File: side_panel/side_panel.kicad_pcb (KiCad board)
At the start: 2 copper layers, 88 parts, among them CN4 DLL-5569-6AW, CN5 KF2EDGRC-5.08-4P, SW15 KH-6X6X6H-STM, SW16 KH-6X6X6H-STM, U19 PY32F030K28U6TR, U20 WAFER-XH254WZ-2A, U21 WAFER-XH254WZ-2A, U22 WAFER-XH254WZ-4A, U23 KF128-5.08-2P, U24 KF128-5.08-2P, U31 TMC2209-LA, U32 VL53L0CXV0DH1, U33 TPS562201DDCR, U34 SS6285M-SO-TP, U35 SP3485EN, X3 AFA01-S05FCA-00, X4 AFA01-S05FCA-00

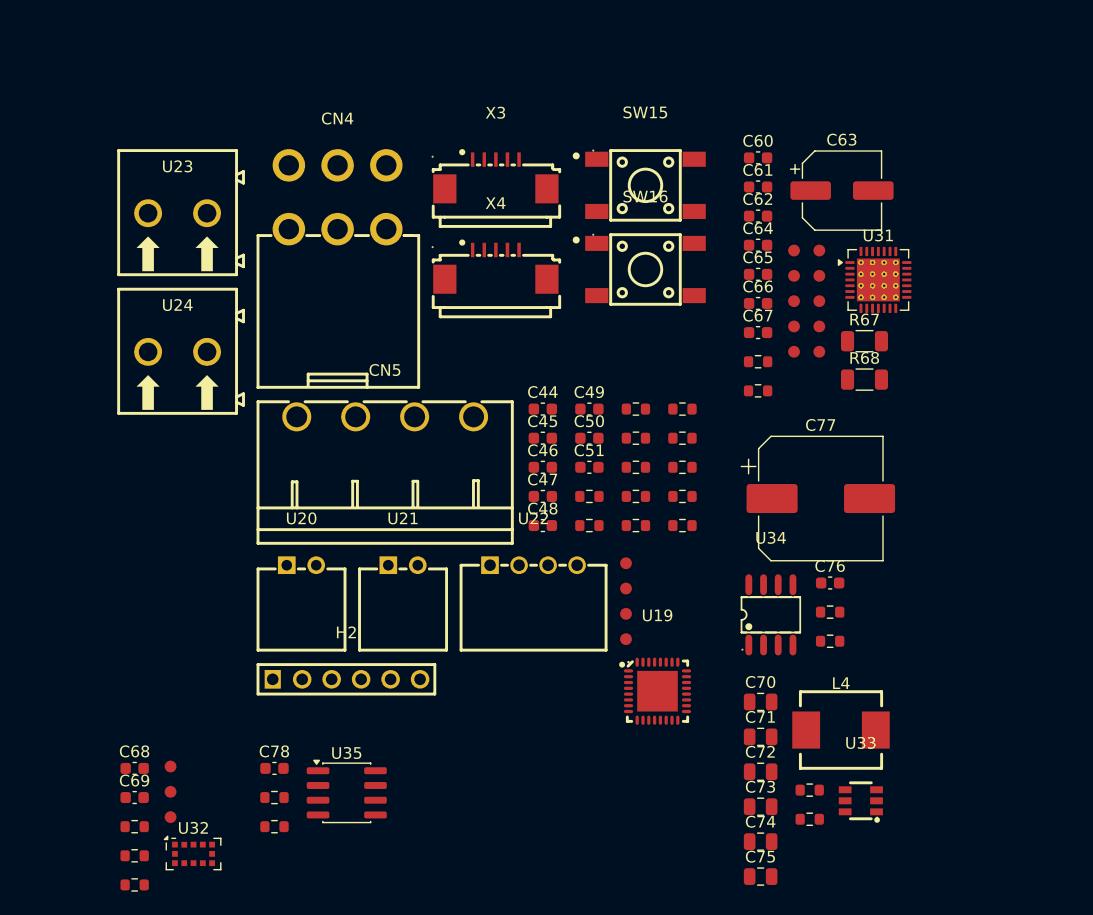
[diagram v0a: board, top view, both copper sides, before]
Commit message: feat: 添加侧电机板基础元件布局
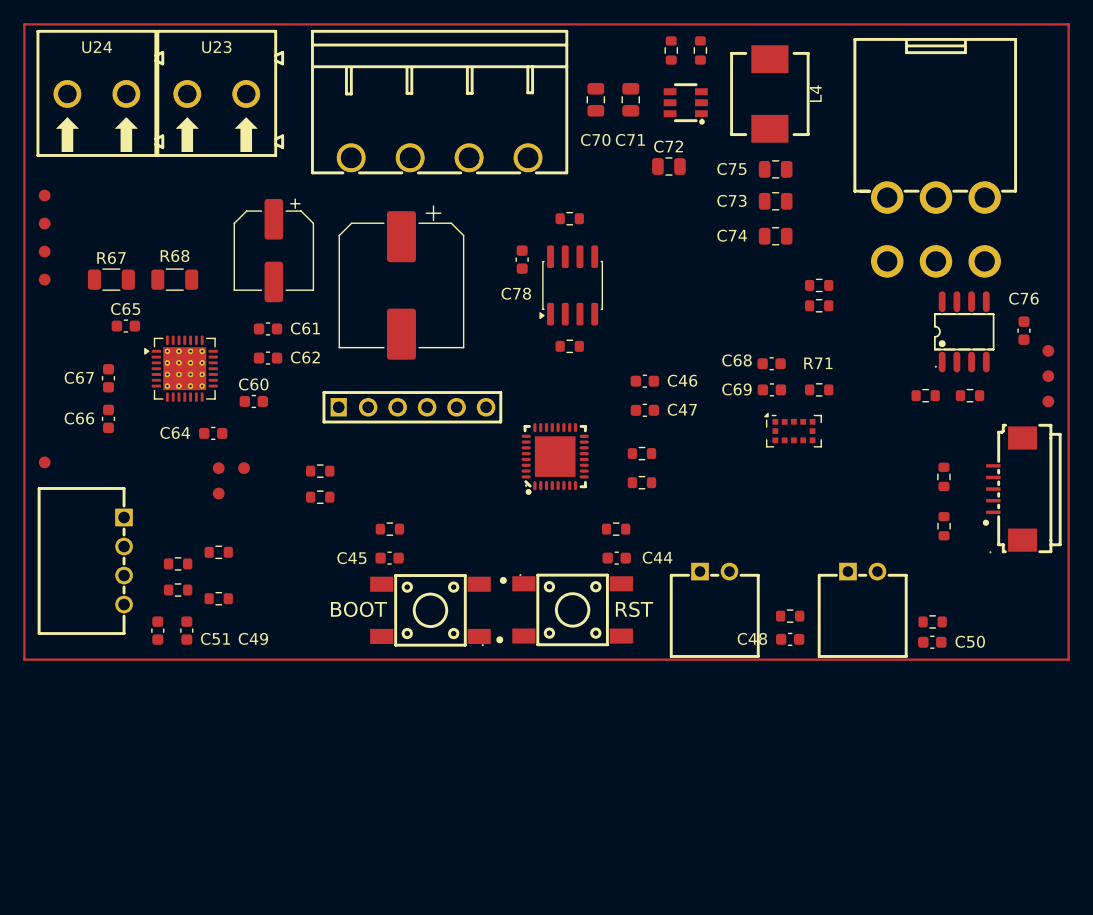
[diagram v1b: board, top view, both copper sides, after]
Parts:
- removed TP14, TP15, TP16, TP17: 1.0mm, PCM_SparkFun-Connector:TestPoint-1.0mm
- removed TP24, TP25: TestPoint, PCM_SparkFun-Connector:TestPoint-1.0mm
- removed X4: AFA01-S05FCA-00, lcsc_footprints:C262753_FPC-SMD_AFA01-S05FCA-00
- moved TP32 83.7 mm to (180.2, 83.4)
- moved TP33 83.7 mm to (180.2, 85.6)
- moved TP34 83.7 mm to (180.2, 87.8)
- moved R69 76.0 mm to (171.2, 94.2), turned to -90 degrees
- moved R70 75.3 mm to (171.3, 98.5), turned to 90 degrees
- moved R71 72.8 mm to (160.5, 86.8)
- moved TP29 67.4 mm to (93.8, 70.0)
- moved TP31 67.3 mm to (93.8, 74.8)
- moved R73 66.9 mm to (150.3, 57.5), turned to 90 degrees
- moved TP28 66.9 mm to (93.8, 72.4)
- moved TP30 66.9 mm to (93.8, 77.2)
- moved TP26 65.3 mm to (93.8, 93.0)
- moved C69 65.2 mm to (156.4, 86.8)
- moved R67 65.1 mm to (99.5, 77.2)
- moved C68 65.0 mm to (156.4, 84.5)
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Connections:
- R65 pad 2: /步进驱动/UART_TX/RX -> /TMC_UART
- R66 pad 1: /步进驱动/EN -> /TMC_EN
- R71 pad 1: /TOF/XSHUT -> /TOF_XSHUT
- TP23 pad 1: /步进驱动/DIR -> /TMC_DIR
- U19 pad 10: /MOTOR_BI -> /TOF_XSHUT
- U19 pad 11: Net-(U19-PA5) -> /SCL
- U19 pad 12: /TMC_STEP -> /SDA
- U19 pad 13: /MOTOR_FI -> /MOTOR_ENC_B
- U19 pad 14: /步进驱动/DIAG -> /MOTOR_ENC_A
- U19 pad 15: Net-(U19-PB1) -> unconnected-(U19-PB1-Pad15)
- U19 pad 17: /RS485_PY32/RS485_DE -> /MOTOR_FI
- U19 pad 18: /EXT_ENC_A -> /MOTOR_BI
- U19 pad 19: /EXT_ENC_B -> unconnected-(U19-PA9-OSC32OUT-Pad19)
- U19 pad 2: /步进驱动/EN -> /EXT_ENC_B
- U19 pad 20: /PUSH_BUTTON_2 -> /RS485_PY32/RS485_TX
- U19 pad 21: /TOF_SCL -> /RS485_PY32/RS485_RX
- U19 pad 22: /TOF_SDA -> /RS485_PY32/RS485_DE
- U19 pad 26: Net-(U19-PB3) -> /TMC_DIAG
- U19 pad 27: /MOTOR_ENC_A -> /TMC_UART
- U19 pad 28: /MOTOR_ENC_B -> /TMC_EN
- U19 pad 29: /RS485_PY32/RS485_TX -> /TMC_DIR
- U19 pad 3: /步进驱动/UART_TX/RX -> /EXT_ENC_A
- U19 pad 30: /RS485_PY32/RS485_RX -> /TMC_STEP
- U19 pad 32: Net-(U19-PB8) -> unconnected-(U19-PB8-Pad32)
- U19 pad 5: /步进驱动/DIR -> /PUSH_BUTTON_1
- U19 pad 7: /TOF_XSHUT -> /PUSH_BUTTON_2
- U19 pad 8: /步进驱动/INDEX -> unconnected-(U19-PA2-Pad8)
- U19 pad 9: /PUSH_BUTTON_1 -> unconnected-(U19-PA3-Pad9)
- U31 pad 11: /步进驱动/DIAG -> /TMC_DIAG
- U31 pad 19: /步进驱动/DIR -> /TMC_DIR
- U31 pad 2: /步进驱动/EN -> /TMC_EN
- U32 pad 5: /TOF/XSHUT -> /TOF_XSHUT
- U34 pad 5: /MOTOR_OUT2 -> /MOTOR_OUT1
- U34 pad 6: /MOTOR_OUT2 -> /MOTOR_OUT1
- U34 pad 7: /MOTOR_OUT1 -> /MOTOR_OUT2
- U34 pad 8: /MOTOR_OUT1 -> /MOTOR_OUT2
- X3 pad 1: /TOF/XSHUT -> /TOF_XSHUT
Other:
- board text added: "BOOT"
- board text added: "RST"

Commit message: update: 更新侧板PCB
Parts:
- moved C64 4.76 mm to (112.2, 87.8), turned to -90 degrees
- moved C60 1.18 mm to (110.6, 87.8), turned to -90 degrees
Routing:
- net /TMC_UART: track 0.00 -> 17.8 mm
- net /SWDIO: track 0.00 -> 15.7 mm
- net /RST: track 0.00 -> 12.8 mm, vias 0 -> 2
- net Net-(U31-~{PD}/UART): track 0.00 -> 12.5 mm
- net /SWCLK: track 0.00 -> 12.3 mm
- net /ISP_RX: track 0.00 -> 7.04 mm
- net /+3V3: track 0.00 -> 4.17 mm
- net /GND: track 0.00 -> 1.60 mm

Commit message: 更新针脚变动
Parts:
- removed CN5: KF2EDGRC-5.08-4P, lcsc_footprints:C441238_CONN-TH_4P-P5_08_KF2EDGRC-5_08-4P
- added CN1: KF2EDGRC-5.08-4P, lcsc_footprints:C441238_CONN-TH_4P-P5_08_KF2EDGRC-5_08-4P, F.Cu at (127.6, 66.8)
- added D1: LED, LED_SMD:LED_0603_1608Metric, F.Cu at (148.6, 74.2)
- added D2: LED, LED_SMD:LED_0603_1608Metric, F.Cu at (148.6, 76.8)
- added R13: 10k, Resistor_SMD:R_0603_1608Metric, F.Cu at (145.0, 74.2)
- added R14: 1k, Resistor_SMD:R_0603_1608Metric, F.Cu at (145.0, 76.7)
- added R15: 1k, Resistor_SMD:R_0603_1608Metric, F.Cu at (145.0, 79.2)
- C1: renamed from C44; value 1uF -> 100nF
- C3: renamed from C45; value 1uF -> 100nF
- R1: renamed from R41; footprint PCM_SparkFun-Resistor:R_0603_1608Metric -> Resistor_SMD:R_0603_1608Metric
- R10: renamed from R52; footprint PCM_SparkFun-Resistor:R_0603_1608Metric -> Resistor_SMD:R_0603_1608Metric
- R11: renamed from R46; footprint PCM_SparkFun-Resistor:R_0603_1608Metric -> Resistor_SMD:R_0603_1608Metric
- R12: renamed from R50; footprint PCM_SparkFun-Resistor:R_0603_1608Metric -> Resistor_SMD:R_0603_1608Metric
- R16: renamed from R72; footprint PCM_SparkFun-Resistor:R_0603_1608Metric -> Resistor_SMD:R_0603_1608Metric
- R17: renamed from R73; footprint PCM_SparkFun-Resistor:R_0603_1608Metric -> Resistor_SMD:R_0603_1608Metric
- R18: renamed from R76; footprint PCM_SparkFun-Resistor:R_0603_1608Metric -> Resistor_SMD:R_0603_1608Metric
- R19: renamed from R77; footprint PCM_SparkFun-Resistor:R_0603_1608Metric -> Resistor_SMD:R_0603_1608Metric
- R2: renamed from R42; footprint PCM_SparkFun-Resistor:R_0603_1608Metric -> Resistor_SMD:R_0603_1608Metric
- R20: renamed from R69; footprint PCM_SparkFun-Resistor:R_0603_1608Metric -> Resistor_SMD:R_0603_1608Metric
- R21: renamed from R70; footprint PCM_SparkFun-Resistor:R_0603_1608Metric -> Resistor_SMD:R_0603_1608Metric
- R22: renamed from R71; footprint PCM_SparkFun-Resistor:R_0603_1608Metric -> Resistor_SMD:R_0603_1608Metric
- R23: renamed from R74; footprint PCM_SparkFun-Resistor:R_0603_1608Metric -> Resistor_SMD:R_0603_1608Metric
- R24: renamed from R75; footprint PCM_SparkFun-Resistor:R_0603_1608Metric -> Resistor_SMD:R_0603_1608Metric
- R25: renamed from R65; footprint PCM_SparkFun-Resistor:R_0603_1608Metric -> Resistor_SMD:R_0603_1608Metric
- R26: renamed from R66; footprint PCM_SparkFun-Resistor:R_0603_1608Metric -> Resistor_SMD:R_0603_1608Metric
- R27: renamed from R67; footprint Resistor_SMD:R_1206_3216Metric -> Resistor_SMD:R_0603_1608Metric
- R28: renamed from R68; footprint Resistor_SMD:R_1206_3216Metric -> Resistor_SMD:R_0603_1608Metric
- R3: renamed from R45; footprint PCM_SparkFun-Resistor:R_0603_1608Metric -> Resistor_SMD:R_0603_1608Metric
- R4: renamed from R47; footprint PCM_SparkFun-Resistor:R_0603_1608Metric -> Resistor_SMD:R_0603_1608Metric
- R5: renamed from R43; footprint PCM_SparkFun-Resistor:R_0603_1608Metric -> Resistor_SMD:R_0603_1608Metric
- R6: renamed from R44; footprint PCM_SparkFun-Resistor:R_0603_1608Metric -> Resistor_SMD:R_0603_1608Metric
- R7: renamed from R48; footprint PCM_SparkFun-Resistor:R_0603_1608Metric -> Resistor_SMD:R_0603_1608Metric
- R8: renamed from R49; footprint PCM_SparkFun-Resistor:R_0603_1608Metric -> Resistor_SMD:R_0603_1608Metric
- R9: renamed from R51; footprint PCM_SparkFun-Resistor:R_0603_1608Metric -> Resistor_SMD:R_0603_1608Metric
- renumbered C71 to C10, C72 to C11, C73 to C12, C74 to C13, C75 to C14, C78 to C15, C68 to C16, C69 to C17, C76 to C18, C77 to C19, C46 to C2, C60 to C20, C61 to C21, C62 to C22, C63 to C23, C64 to C24, C65 to C25, C66 to C26, C67 to C27, C47 to C4, C49 to C5, C51 to C6, C48 to C7, C50 to C8, C70 to C9, CN4 to CN2, H2 to H1, L4 to L1, SW15 to SW1, SW16 to SW2, TP32 to TP1, TP30 to TP10, TP31 to TP11, TP33 to TP2, TP34 to TP3, TP22 to TP4, TP23 to TP5, TP26 to TP6, TP27 to TP7, TP28 to TP8, TP29 to TP9, U23 to U1, U34 to U10, U31 to U11, U24 to U2, U19 to U3, U22 to U4, U20 to U5, U21 to U6, U33 to U7, U35 to U8, U32 to U9, X3 to X1
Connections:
- net /+12V renamed +12V
- net /RS485_PY32/RS485_A renamed /RS485_A
- net /RS485_PY32/RS485_B renamed /RS485_B
- C1 pad 2: /GND -> GND
- C10 pad 2: /GND -> GND
- C12 pad 1: /+3V3 -> +3V3
- C12 pad 2: /GND -> GND
- C13 pad 1: /+3V3 -> +3V3
- C13 pad 2: /GND -> GND
- C14 pad 1: /+3V3 -> +3V3
- C14 pad 2: /GND -> GND
- C15 pad 1: /+3V3 -> +3V3
- C15 pad 2: /GND -> GND
- C16 pad 1: /TOF/+3V3 -> +3V3
- C16 pad 2: /TOF/GND -> GND
- C17 pad 1: /TOF/+3V3 -> +3V3
- C17 pad 2: /TOF/GND -> GND
- C18 pad 2: /GND -> GND
- C19 pad 2: /GND -> GND
- C2 pad 1: /GND -> GND
- C2 pad 2: /+3V3 -> +3V3
- C20 pad 1: /+3V3 -> +3V3
- C20 pad 2: /GND -> GND
- C21 pad 2: /GND -> GND
- C22 pad 2: /GND -> GND
- C23 pad 2: /GND -> GND
- C24 pad 1: /+3V3 -> +3V3
- C24 pad 2: /GND -> GND
- C26 pad 2: /GND -> GND
- C3 pad 2: /GND -> GND
- C4 pad 1: /GND -> GND
- C4 pad 2: /+3V3 -> +3V3
- C5 pad 2: /GND -> GND
- C6 pad 2: /GND -> GND
- C7 pad 2: /GND -> GND
- C8 pad 2: /GND -> GND
- C9 pad 2: /GND -> GND
- CN2 pad 1: /+3V3 -> +3V3
- CN2 pad 3: /GND -> GND
- H1 pad 1: /+3V3 -> +3V3
- H1 pad 2: /GND -> GND
- L1 pad 2: /+3V3 -> +3V3
- R1 pad 1: /+3V3 -> +3V3
- R11 pad 2: /GND -> GND
- R12 pad 2: /GND -> GND
- R16 pad 2: /+3V3 -> +3V3
- R17 pad 1: /GND -> GND
- R18 pad 2: /GND -> GND
- R2 pad 2: /GND -> GND
- R20 pad 1: /TOF/+3V3 -> +3V3
- R20 pad 2: /TOF/SDA -> /SDA
- R21 pad 1: /TOF/+3V3 -> +3V3
- R21 pad 2: /TOF/SCL -> /SCL
- R22 pad 2: /TOF/GND -> GND
- R23 pad 1: /GND -> GND
- R24 pad 1: /GND -> GND
- R26 pad 2: /+3V3 -> +3V3
- R27 pad 2: /GND -> GND
- R28 pad 2: /GND -> GND
- R5 pad 1: /+3V3 -> +3V3
- R6 pad 2: /GND -> GND
- R7 pad 1: /+3V3 -> +3V3
- R8 pad 1: /+3V3 -> +3V3
- SW1 pad 4: /GND -> GND
- SW2 pad 2: /+3V3 -> +3V3
- TP1 pad 1: /TOF/SCL -> /SCL
- TP2 pad 1: /TOF/SDA -> /SDA
- U10 pad 3: /GND -> GND
- U11 pad 10: /GND -> GND
- U11 pad 13: /GND -> GND
- U11 pad 15: /+3V3 -> +3V3
- U11 pad 18: /GND -> GND
- U11 pad 20: /GND -> GND
- U11 pad 29: /GND -> GND
- U11 pad 3: /GND -> GND
- U11 pad 7: /GND -> GND
- U11 pad 9: /GND -> GND
- U3 pad 1: /+3V3 -> +3V3
- U3 pad 16: /GND -> GND
- U3 pad 33: /GND -> GND
- U4 pad 1: /+3V3 -> +3V3
- U4 pad 2: /GND -> GND
- U5 pad 1: /+3V3 -> +3V3
- U6 pad 1: /+3V3 -> +3V3
- U7 pad 1: /GND -> GND
- U8 pad 5: /GND -> GND
- U8 pad 8: /+3V3 -> +3V3
- U9 pad 1: /TOF/+3V3 -> +3V3
- U9 pad 10: /TOF/SCL -> /SCL
- U9 pad 11: /TOF/+3V3 -> +3V3
- U9 pad 12: /TOF/GND -> GND
- U9 pad 2: /TOF/GND -> GND
- U9 pad 3: /TOF/GND -> GND
- U9 pad 4: /TOF/GND -> GND
- U9 pad 6: /TOF/GND -> GND
- U9 pad 9: /TOF/SDA -> /SDA
- X1 pad 2: /TOF/SCL -> /SCL
- X1 pad 3: /TOF/SDA -> /SDA
- X1 pad 4: /TOF/+3V3 -> +3V3
- X1 pad 5: /TOF/GND -> GND
- X1 pad 6: /TOF/GND -> unconnected-(X1-Pad6)
- X1 pad 7: /TOF/GND -> unconnected-(X1-Pad7)
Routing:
- net /+3V3: track 4.17 -> 0.00 mm
- net +3V3: track 0.00 -> 4.17 mm
- net GND: track 0.00 -> 1.60 mm
- net /GND: track 1.60 -> 0.00 mm
